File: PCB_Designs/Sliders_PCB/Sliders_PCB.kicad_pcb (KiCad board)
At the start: 2 copper layers, 7 parts, among them P1 CONN_01X06

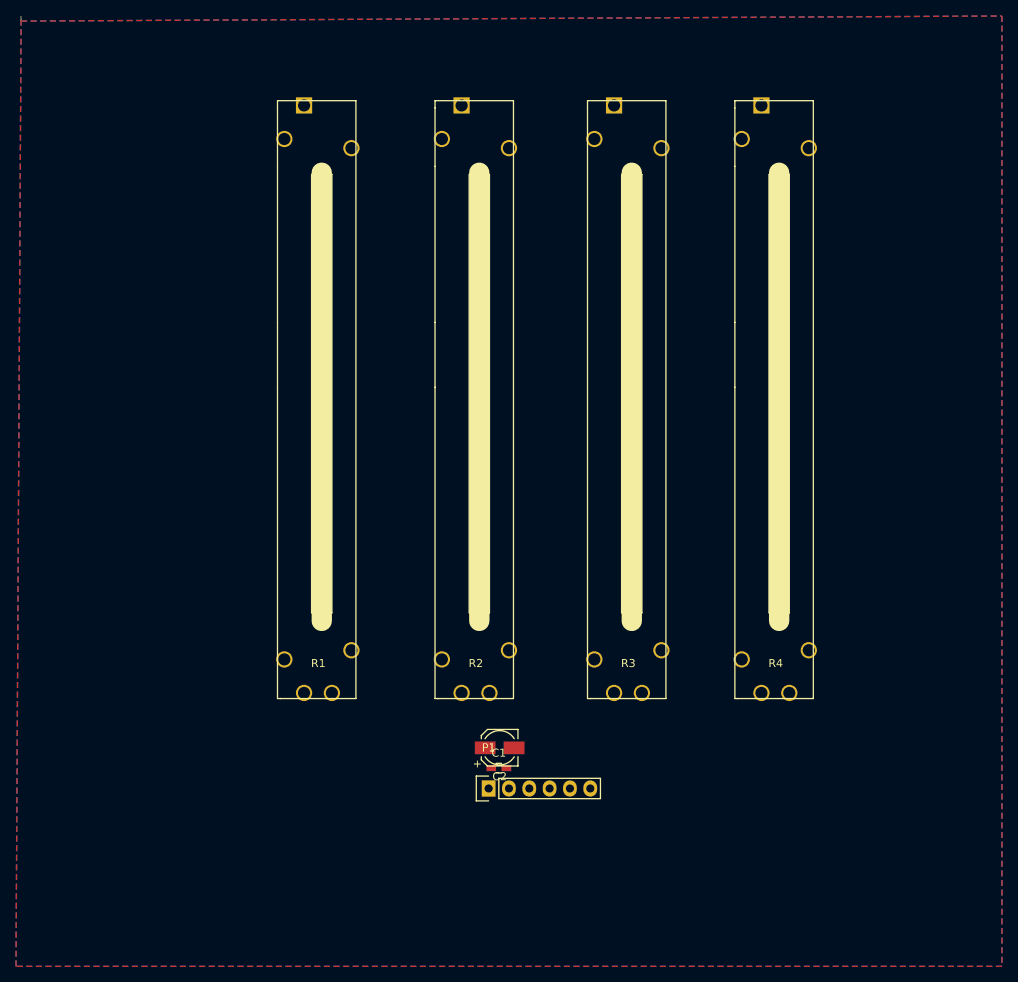
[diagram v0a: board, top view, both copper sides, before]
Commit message: PTA6043, Sliders_PCB
Added:
PTA 6043 .lib and .pretty

Drew traces to Sliders_PCB (v1)
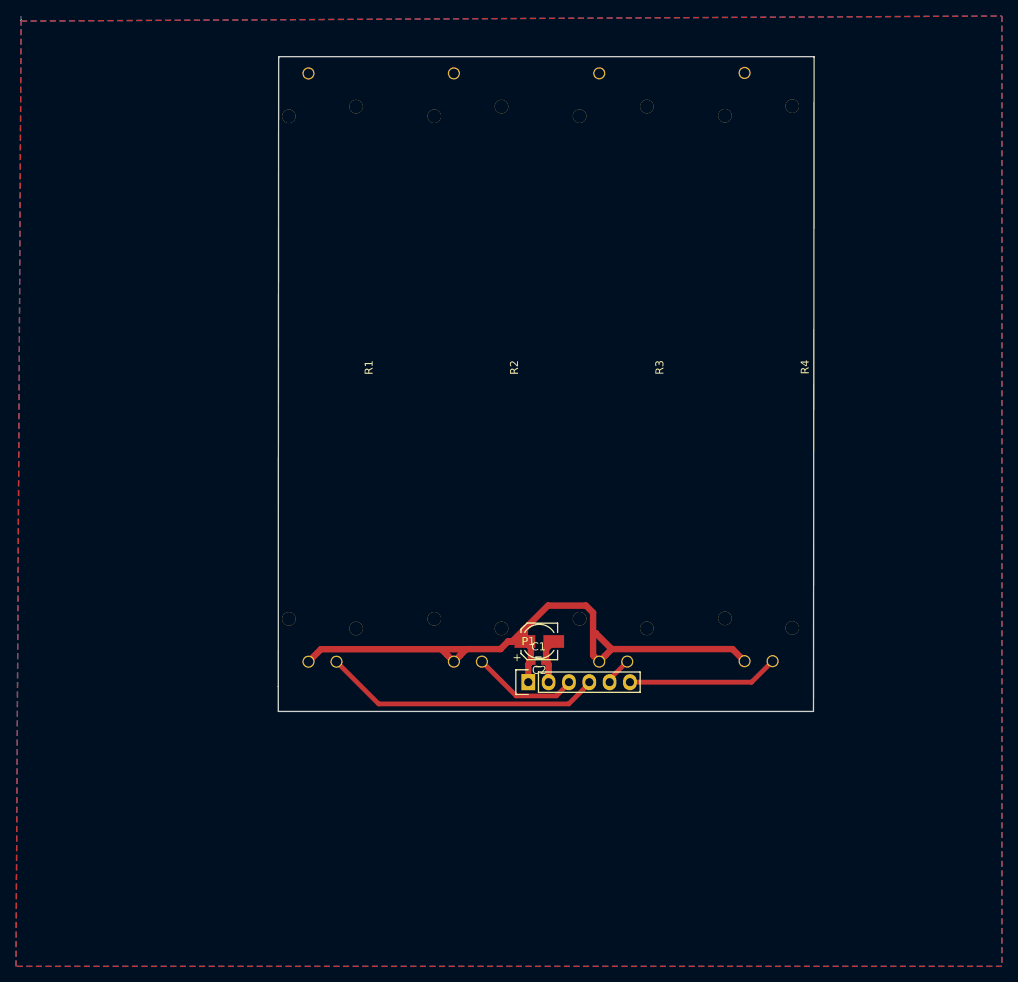
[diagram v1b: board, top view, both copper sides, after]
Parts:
- R1, R2, R3, R4: value 10k -> PTA6043; footprint PTA6043:PTA6043 -> Potentiometers_Bourne:Potentiometer_Bourns-PTA6043
- moved C1 14.2 mm to (132.0, 101.7)
- moved C2 14.2 mm to (132.1, 99.1)
- moved P1 14.2 mm to (130.7, 104.2)
- moved R4 6.85 mm to (157.7, 101.6), turned to 90 degrees
- moved R3 6.62 mm to (139.5, 101.6), turned to 90 degrees
- moved R2 5.92 mm to (121.4, 101.6), turned to 90 degrees
- moved R1 4.88 mm to (103.2, 101.6), turned to 90 degrees
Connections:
- R1 pad 2: Net-(P1-Pad3) -> Net-(P1-Pad4)
- R2 pad 2: Net-(P1-Pad4) -> Net-(P1-Pad3)
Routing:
- net /VDD: track 0.00 -> 81.5 mm
- net Net-(P1-Pad4): track 0.00 -> 35.0 mm
- net Net-(P1-Pad6): track 0.00 -> 18.9 mm
- net Net-(P1-Pad3): track 0.00 -> 13.4 mm
- net /GND: track 0.00 -> 5.61 mm
- net Net-(P1-Pad5): track 0.00 -> 3.49 mm
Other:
- board outline added: 67 x 81.8 mm
- net class Default: clearance 0.2 -> 0.4; trace_width 0.25 -> 0.5; via_dia 0.6 -> 0.8; via_drill 0.4 -> 0.6
- rule trace_clearance: 0.2 -> 0.4
- rule via_min_drill: 0.3 -> 0.6

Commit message: Sliders v2
Sliders_PCB klara
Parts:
- removed C2: CP, Capacitors_SMD:CP_Elec_4x4.5
- moved P1 20.8 mm to (109.9, 104.2)
- moved C1 20.7 mm to (111.3, 101.9)
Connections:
- R1 pad 2: Net-(P1-Pad4) -> Net-(P1-Pad3)
- R2 pad 2: Net-(P1-Pad3) -> Net-(P1-Pad4)
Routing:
- net Net-(P1-Pad5): track 3.49 -> 29.6 mm
- net Net-(P1-Pad4): track 35.0 -> 12.4 mm
- net Net-(P1-Pad6): track 18.9 -> 39.7 mm
- net /VDD: track 81.5 -> 76.3 mm
- net /GND: track 5.61 -> 2.39 mm
- net Net-(P1-Pad3): track 13.4 -> 11.1 mm
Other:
- board size 67 x 81.8 mm -> 67.1 x 80.5 mm

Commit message: Buttons_V3, Sliders_V2
Easier to manufacture External PCB designs finalized.
Uneccesary footprints library added "Connectors" (Could not find the
regular connector FP, turns out it's the socket-strips)
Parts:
- moved C1 5.72 mm to (117.0, 101.9)
- moved P1 5.72 mm to (115.6, 104.2)
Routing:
- net Net-(P1-Pad5): track 29.6 -> 20.3 mm
- net Net-(P1-Pad4): track 12.4 -> 3.26 mm
- net Net-(P1-Pad3): track 11.1 -> 17.6 mm
- net Net-(P1-Pad6): track 39.7 -> 34.0 mm
- net /VDD: track 76.3 -> 81.8 mm
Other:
- net class Default: clearance 0.4 -> 0.5; trace_width 0.5 -> 0.7; via_dia 0.8 -> 1; via_drill 0.6 -> 0.8
- rule trace_clearance: 0.4 -> 0.5
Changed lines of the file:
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@@
   (general
     (links 14)
-    (no_connects 8)
-    (area 99.391399 25.959999 166.470401 107.923401)
+    (no_connects 9)
+    (area 66.675 18.806699 189.865001 139.700001)
     (thickness 1.6)
     (drawings 7)
-    (tracks 47)
+    (tracks 37)
     (zones 0)
     (modules 6)
@@
     (user_trace_width 1)
     (user_trace_width 1.2)
-    (trace_clearance 0.4)
+    (trace_clearance 0.5)
     (zone_clearance 0.508)
     (zone_45_only no)
@@
     (segment_width 0.2)
     (edge_width 0.15)
-    (via_size 0.8)
-    (via_drill 0.6)
+    (via_size 1)
+    (via_drill 0.8)
     (via_min_size 0.8)
     (via_min_drill 0.6)
@@
   (net 6 "Net-(P1-Pad6)")
   (net_class Default "This is the default net class."
-    (clearance 0.4)
-    (trace_width 0.5)
-    (via_dia 0.8)
-    (via_drill 0.6)
+    (clearance 0.5)
+    (trace_width 0.7)
+    (via_dia 1)
+    (via_drill 0.8)
     (uvia_dia 0.3)
     (uvia_drill 0.1)
@@
   )
   (module Capacitors_SMD:C_0603_HandSoldering (layer F.Cu)
-    (at 111.2774 101.8794)
+    (at 116.9924 101.8794)
     (descr "Capacitor SMD 0603, hand soldering")
     (tags "capacitor 0603")
@@
   )
   (module Socket_Strips:Socket_Strip_Straight_1x06 (layer F.Cu)
-    (at 109.8804 104.1908)
+    (at 115.5954 104.1908)
     (descr "Through hole socket strip")
     (tags "socket strip")
@@
     (arrow2b (pts (xy 99.06 26.035) (xy 100.186504 25.448579)))
   )
-  (segment (start 119.832599 100.071399) (end 122.940601 100.071399) (width 0.8) (layer B.Cu) (net 1))
-  (segment (start 122.940601 100.071399) (end 122.956201 100.055799) (width 0.8) (layer B.Cu) (net 1))
-  (segment (start 121.3866 101.6254) (end 119.832599 100.071399) (width 0.8) (layer B.Cu) (net 1))
-  (segment (start 119.832599 100.071399) (end 104.781201 100.071399) (width 0.8) (layer B.Cu) (net 1))
-  (segment (start 104.781201 100.071399) (end 103.981199 100.871401) (width 0.8) (layer B.Cu) (net 1))
-  (segment (start 103.981199 100.871401) (end 103.2192 101.6334) (width 0.8) (layer B.Cu) (net 1))
-  (segment (start 141.109601 100.055799) (end 142.0368 100.055799) (width 0.8) (layer B.Cu) (net 1))
-  (segment (start 142.0368 100.055799) (end 156.197399 100.055799) (width 0.8) (layer B.Cu) (net 1))
-  (segment (start 137.985599 100.055799) (end 142.0368 100.055799) (width 0.8) (layer B.Cu) (net 1))
-  (segment (start 139.5476 101.6178) (end 141.109601 100.055799) (width 0.8) (layer B.Cu) (net 1))
-  (segment (start 156.197399 100.055799) (end 156.946601 100.805001) (width 0.8) (layer B.Cu) (net 1))
-  (segment (start 156.946601 100.805001) (end 157.7086 101.567) (width 0.8) (layer B.Cu) (net 1))
-  (segment (start 121.3866 101.6254) (end 122.956201 100.055799) (width 0.8) (layer B.Cu) (net 1))
-  (segment (start 122.956201 100.055799) (end 137.985599 100.055799) (width 0.8) (layer B.Cu) (net 1))
-  (segment (start 137.985599 100.055799) (end 138.785601 100.855801) (width 0.8) (layer B.Cu) (net 1))
-  (segment (start 138.785601 100.855801) (end 139.5476 101.6178) (width 0.8) (layer B.Cu) (net 1))
-  (segment (start 110.3274 101.8794) (end 108.9274 101.8794) (width 0.8) (layer F.Cu) (net 1))
-  (segment (start 108.9274 101.8794) (end 107.611399 103.195401) (width 0.8) (layer F.Cu) (net 1))
-  (segment (start 107.611399 103.195401) (end 104.781201 103.195401) (width 0.8) (layer F.Cu) (net 1))
-  (segment (start 104.781201 103.195401) (end 103.981199 102.395399) (width 0.8) (layer F.Cu) (net 1))
-  (segment (start 103.981199 102.395399) (end 103.2192 101.6334) (width 0.8) (layer F.Cu) (net 1))
-  (segment (start 109.8804 104.1908) (end 109.8804 102.3264) (width 0.8) (layer F.Cu) (net 1))
-  (segment (start 109.8804 102.3264) (end 110.3274 101.8794) (width 0.8) (layer F.Cu) (net 1))
-  (segment (start 112.4204 104.1908) (end 112.4204 102.0724) (width 0.8) (layer F.Cu) (net 2))
-  (segment (start 112.4204 102.0724) (end 112.2274 101.8794) (width 0.8) (layer F.Cu) (net 2))
-  (segment (start 106.7192 101.6334) (end 107.57321 100.77939) (width 0.6) (layer F.Cu) (net 3))
-  (segment (start 107.57321 100.77939) (end 113.362392 100.77939) (width 0.6) (layer F.Cu) (net 3))
-  (segment (start 113.362392 100.77939) (end 114.9604 102.377398) (width 0.6) (layer F.Cu) (net 3))
-  (segment (start 114.9604 102.377398) (end 114.9604 102.5748) (width 0.6) (layer F.Cu) (net 3))
-  (segment (start 114.9604 102.5748) (end 114.9604 104.1908) (width 0.6) (layer F.Cu) (net 3))
-  (segment (start 124.8866 100.54777) (end 124.8866 101.6254) (width 0.6) (layer F.Cu) (net 4))
-  (segment (start 120.270621 99.163388) (end 123.502218 99.163388) (width 0.6) (layer F.Cu) (net 4))
-  (segment (start 123.502218 99.163388) (end 124.8866 100.54777) (width 0.6) (layer F.Cu) (net 4))
-  (segment (start 117.5004 101.933609) (end 120.270621 99.163388) (width 0.6) (layer F.Cu) (net 4))
-  (segment (start 117.5004 104.1908) (end 117.5004 101.933609) (width 0.6) (layer F.Cu) (net 4))
-  (segment (start 120.0404 104.1908) (end 120.0404 102.5748) (width 0.6) (layer F.Cu) (net 5))
-  (segment (start 120.0404 102.5748) (end 119.924599 102.458999) (width 0.6) (layer F.Cu) (net 5))
-  (segment (start 120.684839 100.163399) (end 122.667799 100.163399) (width 0.6) (layer F.Cu) (net 5))
-  (segment (start 119.924599 102.458999) (end 119.924599 100.923639) (width 0.6) (layer F.Cu) (net 5))
-  (segment (start 119.924599 100.923639) (end 120.684839 100.163399) (width 0.6) (layer F.Cu) (net 5))
-  (segment (start 123.908879 103.087401) (end 141.577999 103.087401) (width 0.6) (layer F.Cu) (net 5))
-  (segment (start 122.667799 100.163399) (end 123.1138 100.6094) (width 0.6) (layer F.Cu) (net 5))
-  (segment (start 123.1138 100.6094) (end 123.1138 102.292322) (width 0.6) (layer F.Cu) (net 5))
-  (segment (start 123.1138 102.292322) (end 123.908879 103.087401) (width 0.6) (layer F.Cu) (net 5))
-  (segment (start 141.577999 103.087401) (end 143.0476 101.6178) (width 0.6) (layer F.Cu) (net 5))
-  (segment (start 122.5804 104.1908) (end 158.5848 104.1908) (width 0.6) (layer F.Cu) (net 6))
-  (segment (start 158.5848 104.1908) (end 161.2086 101.567) (width 0.6) (layer F.Cu) (net 6))
+  (segment (start 109.8804 104.1908) (end 115.5954 104.1908) (width 1) (layer B.Cu) (net 1))
+  (segment (start 123.148601 99.863399) (end 137.793199 99.863399) (width 1) (layer B.Cu) (net 1))
+  (segment (start 115.5954 104.1908) (end 115.5954 102.3264) (width 0.8) (layer F.Cu) (net 1))
+  (segment (start 115.5954 102.3264) (end 116.0424 101.8794) (width 0.8) (layer F.Cu) (net 1))
+  (segment (start 103.2192 101.6334) (end 105.7766 104.1908) (width 1) (layer B.Cu) (net 1))
+  (segment (start 105.7766 104.1908) (end 109.8804 104.1908) (width 1) (layer B.Cu) (net 1))
+  (segment (start 119.632599 99.871399) (end 123.140601 99.871399) (width 1) (layer B.Cu) (net 1))
+  (segment (start 123.140601 99.871399) (end 123.148601 99.863399) (width 1) (layer B.Cu) (net 1))
+  (segment (start 141.309601 99.855799) (end 137.800799 99.855799) (width 1) (layer B.Cu) (net 1))
+  (segment (start 137.800799 99.855799) (end 137.793199 99.863399) (width 1) (layer B.Cu) (net 1))
+  (segment (start 139.5476 101.6178) (end 141.309601 99.855799) (width 1) (layer B.Cu) (net 1))
+  (segment (start 141.309601 99.855799) (end 155.997399 99.855799) (width 1) (layer B.Cu) (net 1))
+  (segment (start 155.997399 99.855799) (end 156.946601 100.805001) (width 1) (layer B.Cu) (net 1))
+  (segment (start 156.946601 100.805001) (end 157.7086 101.567) (width 1) (layer B.Cu) (net 1))
+  (segment (start 121.3866 101.6254) (end 123.148601 99.863399) (width 1) (layer B.Cu) (net 1))
+  (segment (start 137.793199 99.863399) (end 138.785601 100.855801) (width 1) (layer B.Cu) (net 1))
+  (segment (start 138.785601 100.855801) (end 139.5476 101.6178) (width 1) (layer B.Cu) (net 1))
+  (segment (start 103.2192 101.6334) (end 104.981201 99.871399) (width 1) (layer B.Cu) (net 1))
+  (segment (start 104.981201 99.871399) (end 119.632599 99.871399) (width 1) (layer B.Cu) (net 1))
+  (segment (start 120.624601 100.863401) (end 121.3866 101.6254) (width 1) (layer B.Cu) (net 1))
+  (segment (start 119.632599 99.871399) (end 120.624601 100.863401) (width 1) (layer B.Cu) (net 1))
+  (segment (start 118.1354 104.1908) (end 118.1354 102.0724) (width 0.8) (layer F.Cu) (net 2))
+  (segment (start 118.1354 102.0724) (end 117.9424 101.8794) (width 0.8) (layer F.Cu) (net 2))
+  (segment (start 106.7192 101.6334) (end 108.302 100.0506) (width 0.8) (layer F.Cu) (net 3))
+  (segment (start 120.6754 104.084279) (end 120.6754 104.1908) (width 0.8) (layer F.Cu) (net 3))
+  (segment (start 108.302 100.0506) (end 118.708602 100.0506) (width 0.8) (layer F.Cu) (net 3))
+  (segment (start 118.708602 100.0506) (end 119.442401 100.784399) (width 0.8) (layer F.Cu) (net 3))
+  (segment (start 119.442401 100.784399) (end 119.442401 102.85128) (width 0.8) (layer F.Cu) (net 3))
+  (segment (start 119.442401 102.85128) (end 120.6754 104.084279) (width 0.8) (layer F.Cu) (net 3))
+  (segment (start 123.2154 104.1908) (end 123.2154 103.2966) (width 0.8) (layer F.Cu) (net 4))
+  (segment (start 123.2154 103.2966) (end 124.8866 101.6254) (width 0.8) (layer F.Cu) (net 4))
+  (segment (start 130.3782 99.4156) (end 140.8454 99.4156) (width 0.8) (layer F.Cu) (net 5))
+  (segment (start 140.8454 99.4156) (end 143.0476 101.6178) (width 0.8) (layer F.Cu) (net 5))
+  (segment (start 125.7554 104.1908) (end 125.7554 104.0384) (width 0.8) (layer F.Cu) (net 5))
+  (segment (start 125.7554 104.0384) (end 130.3782 99.4156) (width 0.8) (layer F.Cu) (net 5))
+  (segment (start 128.2954 104.1908) (end 158.5848 104.1908) (width 0.8) (layer F.Cu) (net 6))
+  (segment (start 158.5848 104.1908) (end 161.2086 101.567) (width 0.8) (layer F.Cu) (net 6))
   (zone (net 2) (net_name /GND) (layer F.Cu) (hatch edge 0.508)
     (connect_pads (clearance 0.508))

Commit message: Main_PCB V1 Complete
Minor changes to everything.
Main_PCB complete with traces and design.
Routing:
- net /GND: track 2.39 -> 7.40 mm, vias 0 -> 1
- net Net-(P1-Pad3): track 17.6 -> 20.4 mm
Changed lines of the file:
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@@
   (general
     (links 14)
-    (no_connects 9)
+    (no_connects 0)
     (area 66.675 18.806699 189.865001 139.700001)
     (thickness 1.6)
     (drawings 7)
-    (tracks 37)
+    (tracks 41)
     (zones 0)
     (modules 6)
@@
   )
   (setup
-    (last_trace_width 0.8)
+    (last_trace_width 1)
     (user_trace_width 0.5)
     (user_trace_width 0.6)
@@
     (arrow2b (pts (xy 99.06 26.035) (xy 100.186504 25.448579)))
   )
+  (segment (start 103.2192 101.6334) (end 104.981201 99.871399) (width 1) (layer B.Cu) (net 1))
+  (segment (start 104.981201 99.871399) (end 119.632599 99.871399) (width 1) (layer B.Cu) (net 1))
   (segment (start 109.8804 104.1908) (end 115.5954 104.1908) (width 1) (layer B.Cu) (net 1))
   (segment (start 123.148601 99.863399) (end 137.793199 99.863399) (width 1) (layer B.Cu) (net 1))
@@
   (segment (start 137.793199 99.863399) (end 138.785601 100.855801) (width 1) (layer B.Cu) (net 1))
   (segment (start 138.785601 100.855801) (end 139.5476 101.6178) (width 1) (layer B.Cu) (net 1))
-  (segment (start 103.2192 101.6334) (end 104.981201 99.871399) (width 1) (layer B.Cu) (net 1))
-  (segment (start 104.981201 99.871399) (end 119.632599 99.871399) (width 1) (layer B.Cu) (net 1))
   (segment (start 120.624601 100.863401) (end 121.3866 101.6254) (width 1) (layer B.Cu) (net 1))
   (segment (start 119.632599 99.871399) (end 120.624601 100.863401) (width 1) (layer B.Cu) (net 1))
+  (via (at 114.8588 98.1456) (size 1) (drill 0.8) (layers F.Cu B.Cu) (net 2))
+  (segment (start 117.9424 101.8794) (end 117.9424 101.2292) (width 1) (layer F.Cu) (net 2))
+  (segment (start 117.9424 101.2292) (end 114.8588 98.1456) (width 1) (layer F.Cu) (net 2))
   (segment (start 118.1354 104.1908) (end 118.1354 102.0724) (width 0.8) (layer F.Cu) (net 2))
   (segment (start 118.1354 102.0724) (end 117.9424 101.8794) (width 0.8) (layer F.Cu) (net 2))
-  (segment (start 106.7192 101.6334) (end 108.302 100.0506) (width 0.8) (layer F.Cu) (net 3))
   (segment (start 120.6754 104.084279) (end 120.6754 104.1908) (width 0.8) (layer F.Cu) (net 3))
-  (segment (start 108.302 100.0506) (end 118.708602 100.0506) (width 0.8) (layer F.Cu) (net 3))
-  (segment (start 118.708602 100.0506) (end 119.442401 100.784399) (width 0.8) (layer F.Cu) (net 3))
-  (segment (start 119.442401 100.784399) (end 119.442401 102.85128) (width 0.8) (layer F.Cu) (net 3))
   (segment (start 119.442401 102.85128) (end 120.6754 104.084279) (width 0.8) (layer F.Cu) (net 3))
+  (segment (start 119.442401 100.657197) (end 119.442401 102.85128) (width 0.8) (layer F.Cu) (net 3))
+  (segment (start 115.530802 96.745598) (end 119.442401 100.657197) (width 0.8) (layer F.Cu) (net 3))
+  (segment (start 114.186798 96.745598) (end 115.530802 96.745598) (width 0.8) (layer F.Cu) (net 3))
+  (segment (start 109.298996 101.6334) (end 114.186798 96.745598) (width 0.8) (layer F.Cu) (net 3))
+  (segment (start 106.7192 101.6334) (end 109.298996 101.6334) (width 0.8) (layer F.Cu) (net 3))
   (segment (start 123.2154 104.1908) (end 123.2154 103.2966) (width 0.8) (layer F.Cu) (net 4))
   (segment (start 123.2154 103.2966) (end 124.8866 101.6254) (width 0.8) (layer F.Cu) (net 4))
